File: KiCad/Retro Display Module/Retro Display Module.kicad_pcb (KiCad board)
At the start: 2 copper layers, 70 x 100 mm, 155 parts, among them J1 Conn_02x04_Odd_Even, J10 Conn_01x02_Pin, J11 Conn_01x02_Pin, J12 VCC, J13 TX, J14 RX, J15 CFG, J16 SEL, J17 GND, J18 Conn_01x12_Pin, J19 Conn_02x03_Odd_Even, J2 VCC, J20 Conn_01x02_Pin, J21 Conn_01x04_Pin, J22 Conn_01x02_Pin, J23 Conn_01x02_Pin, J24 Conn_01x02_Pin, J25 Conn_01x02_Pin, J26 Conn_01x02_Pin, J27 Conn_02x03_Odd_Even, J28 Conn_01x02_Pin, J29 Conn_01x04_Pin, J3 TX, J30 Conn_01x02_Pin, J31 Conn_02x03_Odd_Even, J32 Conn_01x02_Pin, J33 Conn_02x04_Odd_Even, J34 Conn_02x11_Odd_Even, J4 RX, J5 CFG, J6 SEL, J7 GND, J8 Conn_01x02_Pin, J9 Conn_01x02_Pin, U1 AO3401A, U10 AO3401A, U11 AO3401A, U12 LM358DR2G, U13 AO3401A, U14 AO3401A, U15 AO3401A, U16 AO3401A, U17 MJD44H11J, U18 AO3401A, U19 AO3401A, U2 AO3401A, U20 AO3401A, U21 AO3401A, U3 TS-1187A-B-A-B, U4 AO3401A, U5 STM32G030C8T6, U6 AO3401A, U7 TPS5430DDAR, U8 XC6206P332MR, U9 2N7002, Y1 Crystal

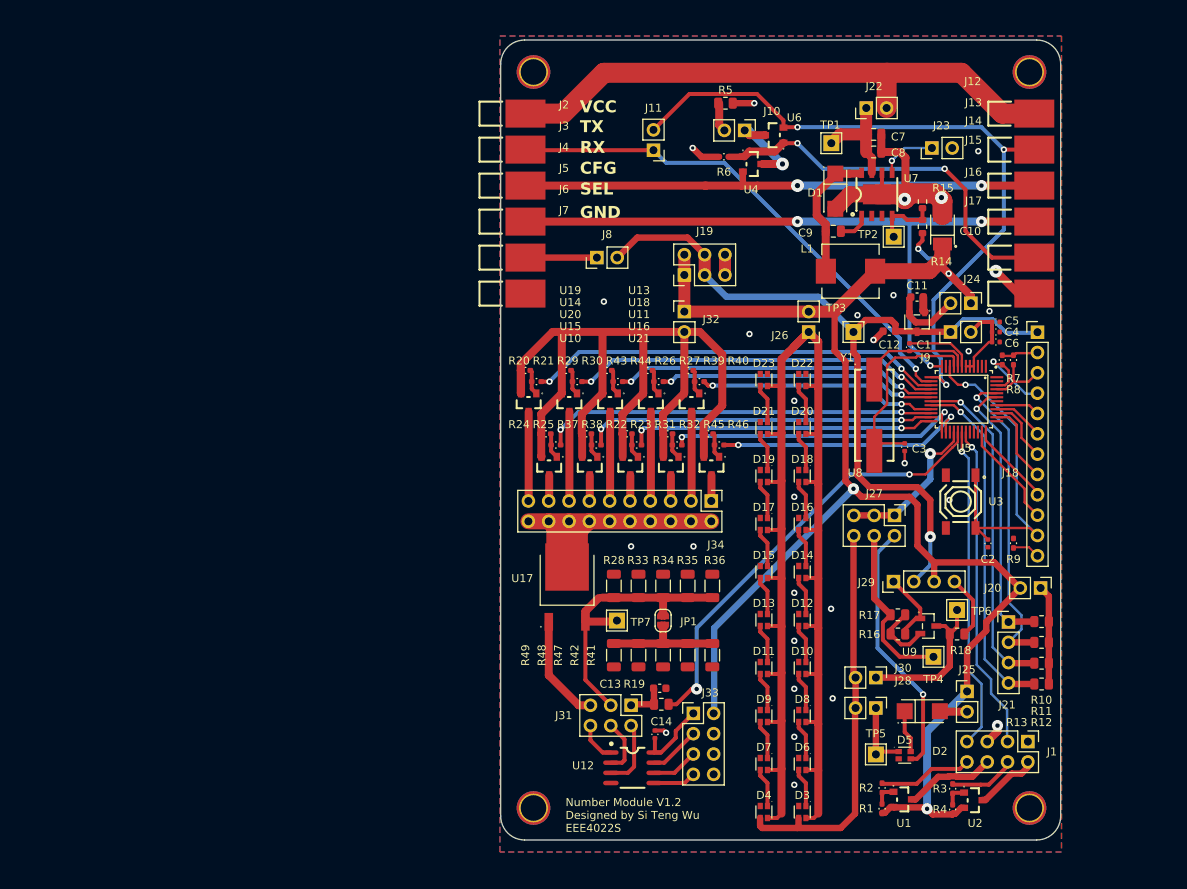
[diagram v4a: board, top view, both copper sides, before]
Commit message: Updated Schematics and Added Reverse polarity protection
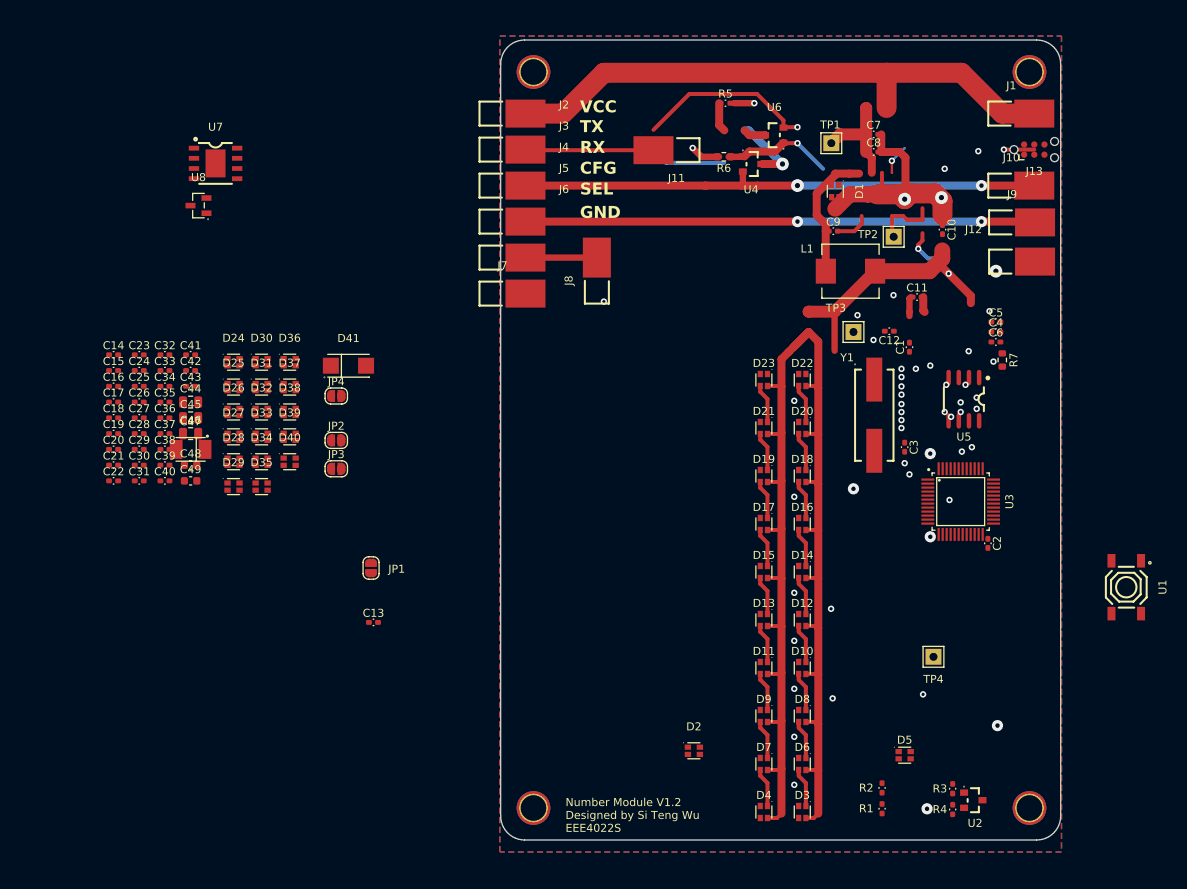
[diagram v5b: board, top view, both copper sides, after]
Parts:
- removed J14: RX, Library:CONN-SMD_YZF0002-38080-02
- removed J15: CFG, Library:CONN-SMD_YZF0002-38080-02
- removed J16: SEL, Library:CONN-SMD_YZF0002-38080-02
- removed J17: GND, Library:CONN-SMD_YZF0002-38080-02
- removed J18: Conn_01x12_Pin, Connector_PinHeader_2.54mm:PinHeader_1x12_P2.54mm_Vertical
- removed J19, J27, J31: Conn_02x03_Odd_Even, Connector_PinHeader_2.54mm:PinHeader_2x03_P2.54mm_Vertical
- removed J20, J22, J23, J24, J25, J26, J28, J30, J32: Conn_01x02_Pin, Connector_PinHeader_2.54mm:PinHeader_1x02_P2.54mm_Vertical
- removed J21, J29: Conn_01x04_Pin, Connector_PinHeader_2.54mm:PinHeader_1x04_P2.54mm_Vertical
- removed J33: Conn_02x04_Odd_Even, Connector_PinHeader_2.54mm:PinHeader_2x04_P2.54mm_Vertical
- removed J34: Conn_02x11_Odd_Even, Connector_PinHeader_2.54mm:PinHeader_2x10_P2.54mm_Vertical
- removed R10, R11, R12, R13: 4.7k, Resistor_SMD:R_0805_2012Metric
- removed R14: 12k, Resistor_SMD:R_0603_1608Metric
- removed R15: 3.9k, Resistor_SMD:R_0603_1608Metric
- removed R16, R17, R18: 1k, Resistor_SMD:R_0805_2012Metric
- removed R19: 10k, Resistor_SMD:R_0805_2012Metric
- removed R20, R22, R24, R26, R29, R31, R37, R39, R43, R45: 100k, Library:R_0402_1005Metric_Pad0.72x0.64mm_HandSolder
- removed R21, R23, R25, R27, R30, R32, R38, R40, R44, R46: 1k, Library:R_0402_1005Metric_Pad0.72x0.64mm_HandSolder
- removed R28, R33, R34, R35, R36, R41, R42, R47, R48, R49: 100, Resistor_SMD:R_1206_3216Metric
- removed R8, R9: 10k, Library:R_0402_1005Metric_Pad0.72x0.64mm_HandSolder
- removed TP5, TP6, TP7: TestPoint, Library:TestPoint_THTPad_2.0x2.0mm_Drill1.0mm
- removed U10, U11, U13, U14, U15, U16, U18, U19, U20, U21: AO3401A, Library:SOT-23_L2.9-W1.3-P1.90-LS2.4-BR
- removed U12: LM358DR2G, Library:Dual LM358
- removed U17: MJD44H11J, Library:MJD44 NPN
- removed U9: 2N7002, Library:SOT-23-3_L2.9-W1.3-P1.90-LS2.4-BR
- added C15: 0.1uF, Library:C_0402_1005Metric_Pad0.74x0.62mm_HandSolder, F.Cu at (67.5, 84.8)
- added C16: 0.1uF, Library:C_0402_1005Metric_Pad0.74x0.62mm_HandSolder, F.Cu at (67.5, 86.8)
- added C17: 0.1uF, Library:C_0402_1005Metric_Pad0.74x0.62mm_HandSolder, F.Cu at (67.5, 88.8)
- added C18: 0.1uF, Library:C_0402_1005Metric_Pad0.74x0.62mm_HandSolder, F.Cu at (67.5, 90.7)
- added C19: 0.1uF, Library:C_0402_1005Metric_Pad0.74x0.62mm_HandSolder, F.Cu at (67.5, 92.7)
- added C20: 0.1uF, Library:C_0402_1005Metric_Pad0.74x0.62mm_HandSolder, F.Cu at (67.5, 94.7)
- added C21: 0.1uF, Library:C_0402_1005Metric_Pad0.74x0.62mm_HandSolder, F.Cu at (67.5, 96.6)
- added C22: 0.1uF, Library:C_0402_1005Metric_Pad0.74x0.62mm_HandSolder, F.Cu at (67.5, 98.6)
- added C23: 0.1uF, Library:C_0402_1005Metric_Pad0.74x0.62mm_HandSolder, F.Cu at (70.7, 82.8)
- added C24: 0.1uF, Library:C_0402_1005Metric_Pad0.74x0.62mm_HandSolder, F.Cu at (70.7, 84.8)
- added C25: 0.1uF, Library:C_0402_1005Metric_Pad0.74x0.62mm_HandSolder, F.Cu at (70.7, 86.8)
- added C26: 0.1uF, Library:C_0402_1005Metric_Pad0.74x0.62mm_HandSolder, F.Cu at (70.7, 88.8)
- added C27: 0.1uF, Library:C_0402_1005Metric_Pad0.74x0.62mm_HandSolder, F.Cu at (70.7, 90.7)
- added C28: 0.1uF, Library:C_0402_1005Metric_Pad0.74x0.62mm_HandSolder, F.Cu at (70.7, 92.7)
- added C29: 0.1uF, Library:C_0402_1005Metric_Pad0.74x0.62mm_HandSolder, F.Cu at (70.7, 94.7)
- added C30: 0.1uF, Library:C_0402_1005Metric_Pad0.74x0.62mm_HandSolder, F.Cu at (70.7, 96.6)
- added C31: 0.1uF, Library:C_0402_1005Metric_Pad0.74x0.62mm_HandSolder, F.Cu at (70.7, 98.6)
- added C32: 0.1uF, Library:C_0402_1005Metric_Pad0.74x0.62mm_HandSolder, F.Cu at (73.9, 82.8)
- added C33: 0.1uF, Library:C_0402_1005Metric_Pad0.74x0.62mm_HandSolder, F.Cu at (73.9, 84.8)
- added C34: 0.1uF, Library:C_0402_1005Metric_Pad0.74x0.62mm_HandSolder, F.Cu at (73.9, 86.8)
- added C35: 0.1uF, Library:C_0402_1005Metric_Pad0.74x0.62mm_HandSolder, F.Cu at (73.9, 88.8)
- added C36: 0.1uF, Library:C_0402_1005Metric_Pad0.74x0.62mm_HandSolder, F.Cu at (73.9, 90.7)
- added C37: 0.1uF, Library:C_0402_1005Metric_Pad0.74x0.62mm_HandSolder, F.Cu at (73.9, 92.7)
- added C38: 0.1uF, Library:C_0402_1005Metric_Pad0.74x0.62mm_HandSolder, F.Cu at (73.9, 94.7)
- added C39: 0.1uF, Library:C_0402_1005Metric_Pad0.74x0.62mm_HandSolder, F.Cu at (73.9, 96.6)
- added C40: 0.1uF, Library:C_0402_1005Metric_Pad0.74x0.62mm_HandSolder, F.Cu at (73.9, 98.6)
- added C41: 0.1uF, Library:C_0402_1005Metric_Pad0.74x0.62mm_HandSolder, F.Cu at (77.1, 82.8)
- added C42: 0.1uF, Library:C_0402_1005Metric_Pad0.74x0.62mm_HandSolder, F.Cu at (77.1, 84.8)
- added C43: 0.1uF, Library:C_0402_1005Metric_Pad0.74x0.62mm_HandSolder, F.Cu at (77.1, 86.8)
- added C44: 4.7uF, Capacitor_SMD:C_0805_2012Metric, F.Cu at (77.1, 88.8)
- added C45: 4.7uF, Capacitor_SMD:C_0805_2012Metric, F.Cu at (77.1, 90.7)
- added C46: 10nF, Capacitor_SMD:C_0805_2012Metric, F.Cu at (77.1, 92.7)
- added C47: 220uF, Library:CAP-SMD_L3.5-W2.8, F.Cu at (77.1, 94.7)
- added C48: 1uF, Capacitor_SMD:C_0603_1608Metric, F.Cu at (77.1, 96.6)
- added C49: 1uF, Capacitor_SMD:C_0603_1608Metric, F.Cu at (77.1, 98.6)
- added D24: XL-1615RGBC-WS2812B, Library:LED-SMD_4P-L1.6-W1.5_XL-1615RGBC-WS2812B, F.Cu at (82.5, 83.8)
- added D25: XL-1615RGBC-WS2812B, Library:LED-SMD_4P-L1.6-W1.5_XL-1615RGBC-WS2812B, F.Cu at (82.5, 86.9)
- added D26: XL-1615RGBC-WS2812B, Library:LED-SMD_4P-L1.6-W1.5_XL-1615RGBC-WS2812B, F.Cu at (82.5, 90.0)
- added D27: XL-1615RGBC-WS2812B, Library:LED-SMD_4P-L1.6-W1.5_XL-1615RGBC-WS2812B, F.Cu at (82.5, 93.1)
- added D28: XL-1615RGBC-WS2812B, Library:LED-SMD_4P-L1.6-W1.5_XL-1615RGBC-WS2812B, F.Cu at (82.5, 96.2)
- added D29: XL-1615RGBC-WS2812B, Library:LED-SMD_4P-L1.6-W1.5_XL-1615RGBC-WS2812B, F.Cu at (82.5, 99.3)
- added D30: XL-1615RGBC-WS2812B, Library:LED-SMD_4P-L1.6-W1.5_XL-1615RGBC-WS2812B, F.Cu at (86.0, 83.8)
- added D31: XL-1615RGBC-WS2812B, Library:LED-SMD_4P-L1.6-W1.5_XL-1615RGBC-WS2812B, F.Cu at (86.0, 86.9)
- added D32: XL-1615RGBC-WS2812B, Library:LED-SMD_4P-L1.6-W1.5_XL-1615RGBC-WS2812B, F.Cu at (86.0, 90.0)
- added D33: XL-1615RGBC-WS2812B, Library:LED-SMD_4P-L1.6-W1.5_XL-1615RGBC-WS2812B, F.Cu at (86.0, 93.1)
- added D34: XL-1615RGBC-WS2812B, Library:LED-SMD_4P-L1.6-W1.5_XL-1615RGBC-WS2812B, F.Cu at (86.0, 96.2)
- added D35: XL-1615RGBC-WS2812B, Library:LED-SMD_4P-L1.6-W1.5_XL-1615RGBC-WS2812B, F.Cu at (86.0, 99.3)
- added D36: XL-1615RGBC-WS2812B, Library:LED-SMD_4P-L1.6-W1.5_XL-1615RGBC-WS2812B, F.Cu at (89.5, 83.8)
- added D37: XL-1615RGBC-WS2812B, Library:LED-SMD_4P-L1.6-W1.5_XL-1615RGBC-WS2812B, F.Cu at (89.5, 86.9)
- added D38: XL-1615RGBC-WS2812B, Library:LED-SMD_4P-L1.6-W1.5_XL-1615RGBC-WS2812B, F.Cu at (89.5, 90.0)
- added D39: XL-1615RGBC-WS2812B, Library:LED-SMD_4P-L1.6-W1.5_XL-1615RGBC-WS2812B, F.Cu at (89.5, 93.1)
- added D40: XL-1615RGBC-WS2812B, Library:LED-SMD_4P-L1.6-W1.5_XL-1615RGBC-WS2812B, F.Cu at (89.5, 96.2)
- added D41: SS34, Library:SMA_L4.3-W2.6-LS5.2-RD, F.Cu at (96.9, 84.2)
- added JP2: Jumper_2_Open, Jumper:SolderJumper-2_P1.3mm_Open_RoundedPad1.0x1.5mm, F.Cu at (95.3, 93.5)
- added JP3: Jumper_2_Open, Jumper:SolderJumper-2_P1.3mm_Open_RoundedPad1.0x1.5mm, F.Cu at (95.3, 97.1)
- added JP4: Jumper_2_Open, Jumper:SolderJumper-2_P1.3mm_Open_RoundedPad1.0x1.5mm, F.Cu at (95.3, 88.0)
- C1, C14, C2, C3, C4: footprint Library:C_0402_1005Metric -> Library:C_0402_1005Metric_Pad0.74x0.62mm_HandSolder
- C10: value 220uF -> 0.1uF; footprint Library:CAP-SMD_L3.5-W2.8 -> Library:C_0402_1005Metric_Pad0.74x0.62mm_HandSolder
- C11, C12, C13: value 1uF -> 0.1uF; footprint Capacitor_SMD:C_0603_1608Metric -> Library:C_0402_1005Metric_Pad0.74x0.62mm_HandSolder
- C5: value 4.7uF -> 0.1uF; footprint Library:C_0402_1005Metric -> Library:C_0402_1005Metric_Pad0.74x0.62mm_HandSolder
- C6: value 0.1uF -> 4.7uF; footprint Library:C_0402_1005Metric -> Library:C_0402_1005Metric_Pad0.74x0.62mm_HandSolder
- C7, C8: value 4.7uF -> 0.1uF; footprint Capacitor_SMD:C_0805_2012Metric -> Library:C_0402_1005Metric_Pad0.74x0.62mm_HandSolder
- C9: value 10nF -> 0.1uF; footprint Capacitor_SMD:C_0805_2012Metric -> Library:C_0402_1005Metric_Pad0.74x0.62mm_HandSolder
- D1: value SS34 -> XL-1615RGBC-WS2812B; footprint Library:SMA_L4.3-W2.6-LS5.2-RD -> Library:LED-SMD_4P-L1.6-W1.5_XL-1615RGBC-WS2812B
- D2: value M7 -> XL-1615RGBC-WS2812B; footprint Library:SMA_L4.3-W2.6-LS5.2-RD -> Library:LED-SMD_4P-L1.6-W1.5_XL-1615RGBC-WS2812B
- J1: value Conn_02x04_Odd_Even -> VCC; footprint Connector_PinHeader_2.54mm:PinHeader_2x04_P2.54mm_Vertical -> Library:CONN-SMD_YZF0002-38080-02
- J10: value Conn_01x02_Pin -> CFG; footprint Connector_PinHeader_2.54mm:PinHeader_1x02_P2.54mm_Vertical -> Library:CONN-SMD_YZF0002-38080-02
- J11: value Conn_01x02_Pin -> SEL; footprint Connector_PinHeader_2.54mm:PinHeader_1x02_P2.54mm_Vertical -> Library:CONN-SMD_YZF0002-38080-02
- J12: value VCC -> GND
- J13: value TX -> Conn_02x03_Odd_Even; footprint Library:CONN-SMD_YZF0002-38080-02 -> Connector:Tag-Connect_TC2030-IDC-NL_2x03_P1.27mm_Vertical
- J2: value VCC -> TX
- J3: value TX -> RX
- J4: value RX -> CFG
- J5: value CFG -> SEL
- J6: value SEL -> GND
- J7: value GND -> VCC
- J8: value Conn_01x02_Pin -> TX; footprint Connector_PinHeader_2.54mm:PinHeader_1x02_P2.54mm_Vertical -> Library:CONN-SMD_YZF0002-38080-02
- J9: value Conn_01x02_Pin -> RX; footprint Connector_PinHeader_2.54mm:PinHeader_1x02_P2.54mm_Vertical -> Library:CONN-SMD_YZF0002-38080-02
- R4: value 100k -> 10k
- R5: footprint Resistor_SMD:R_0805_2012Metric -> Library:R_0402_1005Metric_Pad0.72x0.64mm_HandSolder
- R6: value 100k -> 12k; footprint Library:R_0402_1005Metric_Pad0.72x0.64mm_HandSolder -> Resistor_SMD:R_0603_1608Metric
- R7: value 10k -> 3.9k; footprint Library:R_0402_1005Metric_Pad0.72x0.64mm_HandSolder -> Resistor_SMD:R_0603_1608Metric
- U1: value AO3401A -> TS-1187A-B-A-B; footprint Library:SOT-23_L2.9-W1.3-P1.90-LS2.4-BR -> Library:SW-SMD_4P-L5.1-W5.1-P3.70-LS6.5-TL-2
- U3: value TS-1187A-B-A-B -> STM32G030C8T6; footprint Library:SW-SMD_4P-L5.1-W5.1-P3.70-LS6.5-TL-2 -> Library:LQFP-48_L7.0-W7.0-P0.50-LS9.0-BL_1
- U5: value STM32G030C8T6 -> LM358; footprint Library:LQFP-48_L7.0-W7.0-P0.50-LS9.0-BL_1 -> Library:Dual LM358
- U8: footprint Library:XC6206 -> Library:SOT-23-3_L2.9-W1.3-P1.90-LS2.4-BR
- moved U8 91.0 mm to (78.1, 64.2), turned to 0 degrees
- moved U7 82.8 mm to (80.3, 58.9), turned to 0 degrees
- moved C14 82.6 mm to (67.5, 82.8), turned to 0 degrees
- moved J1 78.5 mm to (182.6, 52.7), turned to 0 degrees
- moved U1 38.5 mm to (194.1, 111.9), turned to -90 degrees
- moved JP1 37.1 mm to (99.7, 109.5)
- moved J10 36.9 mm to (182.6, 61.7), turned to 0 degrees
- moved C13 36.7 mm to (100.0, 116.3)
- moved D2 29.0 mm to (140.0, 132.3)
- moved J12 18.5 mm to (182.7, 71.2)
- moved J9 17.3 mm to (182.7, 66.3), turned to 0 degrees
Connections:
- C1 pad 1: Net-(U5-PF0-OSC_IN) -> Net-(U3-PF0-OSC_IN)
- C11 pad 1: Net-(J24-Pin_2) -> /5V
- C12 pad 1: /3V3 -> /5V
- C13 pad 1: Net-(J31-Pin_1) -> /5V
- C14 pad 1: Net-(J33-Pin_1) -> /5V
- C3 pad 1: Net-(U5-PF1-OSC_OUT) -> Net-(U3-PF1-OSC_OUT)
- C4 pad 1: /VR/B -> /3V3
- C5 pad 1: /VR/B -> Net-(J11-Pin_1)
- C6 pad 1: /VR/B -> /3V3
- C7 pad 1: Net-(J22-Pin_1) -> /3V3
- C8 pad 1: Net-(J22-Pin_1) -> /5V
- C9 pad 1: Net-(D1-K) -> /5V
- C9 pad 2: Net-(U7-BOOT) -> GND
- D1 pad 1: Net-(D1-K) -> Net-(D1-DO)
- D1 pad 2: GND -> /5V
- D10 pad 2: Net-(D10-VDD) -> /5V
- D11 pad 2: Net-(D10-VDD) -> /5V
- D12 pad 2: Net-(D10-VDD) -> /5V
- D12 pad 4: Net-(D10-DO) -> Net-(D12-DI)
- D13 pad 2: Net-(D10-VDD) -> /5V
- D13 pad 4: Net-(D11-DO) -> Net-(D13-DI)
- D14 pad 2: Net-(D10-VDD) -> /5V
- D14 pad 4: Net-(D12-DO) -> Net-(D10-DO)
- D15 pad 2: Net-(D10-VDD) -> /5V
- D15 pad 4: Net-(D13-DO) -> Net-(D11-DO)
- D16 pad 2: Net-(D10-VDD) -> /5V
- D16 pad 4: Net-(D14-DO) -> Net-(D12-DO)
- D17 pad 2: Net-(D10-VDD) -> /5V
- D17 pad 4: Net-(D15-DO) -> Net-(D13-DO)
- D18 pad 2: Net-(D10-VDD) -> /5V
- D18 pad 4: Net-(D16-DO) -> Net-(D14-DO)
- D19 pad 2: Net-(D10-VDD) -> /5V
- D19 pad 4: Net-(D17-DO) -> Net-(D15-DO)
- D2 pad 1: Net-(D2-K) -> Net-(D2-DO)
- D2 pad 2: Net-(D2-A) -> /5V
- D20 pad 2: Net-(D10-VDD) -> /5V
- D20 pad 4: Net-(D18-DO) -> Net-(D16-DO)
- D21 pad 2: Net-(D10-VDD) -> /5V
- D21 pad 4: Net-(D19-DO) -> Net-(D17-DO)
- D22 pad 1: unconnected-(D22-DO-Pad1) -> Net-(D22-DO)
- D22 pad 2: Net-(D10-VDD) -> /5V
- D22 pad 4: Net-(D20-DO) -> Net-(D18-DO)
- D23 pad 1: unconnected-(D23-DO-Pad1) -> Net-(D23-DO)
- D23 pad 2: Net-(D10-VDD) -> /5V
- D23 pad 4: Net-(D21-DO) -> Net-(D19-DO)
- D3 pad 2: Net-(D10-VDD) -> /5V
- D3 pad 4: /RGB LEDs/DIN -> /TIM1_CH1
- D4 pad 2: Net-(D10-VDD) -> /5V
- D4 pad 4: /RGB LEDs/DIN -> /TIM1_CH1
- D5 pad 2: Net-(D2-K) -> /5V
- D5 pad 4: /RGB LEDs/Cheese -> Net-(D1-DO)
- D6 pad 1: Net-(D6-DO) -> Net-(D10-DI)
- D6 pad 2: Net-(D10-VDD) -> /5V
- D6 pad 4: Net-(D3-DO) -> Net-(D2-DO)
- D7 pad 1: Net-(D7-DO) -> Net-(D11-DI)
- D7 pad 2: Net-(D10-VDD) -> /5V
- D7 pad 4: Net-(D4-DO) -> Net-(D3-DO)
- D8 pad 1: Net-(D10-DI) -> Net-(D12-DI)
- D8 pad 2: Net-(D10-VDD) -> /5V
- D8 pad 4: Net-(D6-DO) -> Net-(D4-DO)
- D9 pad 1: Net-(D11-DI) -> Net-(D13-DI)
- D9 pad 2: Net-(D10-VDD) -> /5V
- D9 pad 4: Net-(D7-DO) -> Net-(D5-DO)
- J1 pad 1: GND -> /VCC
- J10 pad 1: Net-(J10-Pin_1) -> /PA1
- J11 pad 1: /USART2_Rx -> Net-(J11-Pin_1)
- J12 pad 1: /VCC -> GND
- J13 pad 1: /USART2_Tx -> /3V3
- J2 pad 1: /VCC -> /USART2_Rx
- J3 pad 1: /USART2_Rx -> Net-(J3-Pin_1)
- J4 pad 1: Net-(J14-Pin_1) -> /PA1
- J5 pad 1: /PA1 -> /3V3
- J6 pad 1: Net-(J6-Pin_1) -> GND
- J7 pad 1: GND -> /VCC
- J8 pad 1: Net-(J6-Pin_1) -> /USART2_Tx
- J9 pad 1: /3V3 -> Net-(J3-Pin_1)
- JP1 pad 1: /LED Driver/-ve -> /5V
- JP1 pad 2: Net-(JP1-B) -> /Power/5V
- L1 pad 1: Net-(D1-K) -> Net-(D41-K)
- L1 pad 2: /5V -> /Power/5V
- R1 pad 1: /5V -> Net-(J11-Pin_1)
- R1 pad 2: Net-(U1-G) -> GND
- R2 pad 1: Net-(U1-G) -> /USART2_Rx
- R2 pad 2: /PC6 -> Net-(U3-PA3)
- R3 pad 1: Net-(U2-G) -> /USART2_Tx
- R3 pad 2: /PC7 -> Net-(U3-PA2)
- R4 pad 1: /5V -> GND
- R4 pad 2: Net-(U2-G) -> /SWDCLK/BOOT
- R5 pad 1: Net-(J10-Pin_2) -> /PA1
- R5 pad 2: GND -> Net-(U3-PA1)
- R6 pad 1: Net-(J16-Pin_1) -> /Power/5V
- R6 pad 2: GND -> Net-(U7-VSENSE)
- R7 pad 1: /I2C_PUR -> Net-(U7-VSENSE)
- R7 pad 2: /I2C1_SDA -> GND
- TP1 pad 1: Net-(J22-Pin_1) -> Net-(U5A-+)
- TP3 pad 1: /3V3 -> /Power/5V
- TP4 pad 1: /RGB LEDs/Level -> /Power/3V3
- U1 pad 1: Net-(U1-G) -> /NRST
- U1 pad 2: /5V -> /NRST
- U1 pad 3: Net-(J1-Pin_6) -> GND
- U2 pad 1: Net-(U2-G) -> Net-(J11-Pin_1)
- U2 pad 2: /5V -> Net-(J3-Pin_1)
- U2 pad 3: Net-(J1-Pin_2) -> Net-(U2-D)
- U3 pad 1: /NRST -> unconnected-(U3-PC13-Pad1)
- U3 pad 2: /NRST -> unconnected-(U3-PC14-OSC32_IN-Pad2)
- U3 pad 3: GND -> unconnected-(U3-PC15-OSC32_OUT-Pad3)
- U3 pad 4: GND -> /3V3
- U4 pad 1: Net-(J16-Pin_1) -> Net-(J11-Pin_1)
- U4 pad 2: Net-(J14-Pin_1) -> /USART2_Tx
- U4 pad 3: Net-(J10-Pin_1) -> Net-(U2-D)
- U5 pad 1: unconnected-(U5-PC13-Pad1) -> Net-(U6-G)
- U5 pad 2: unconnected-(U5-PC14-OSC32_IN-Pad2) -> /Power/VCC
- U5 pad 3: unconnected-(U5-PC15-OSC32_OUT-Pad3) -> Net-(U5A-+)
- U5 pad 4: /VR/B -> GND
- U5 pad 5: /VR/B -> GND
- U5 pad 6: /VR/B -> GND
- U5 pad 7: GND -> unconnected-(U5-Pad7)
- U5 pad 8: Net-(U5-PF0-OSC_IN) -> Net-(U5A-+)
- U6 pad 1: Net-(J16-Pin_1) -> Net-(U6-G)
- U6 pad 2: /USART2_Tx -> Net-(U5A-+)
- U6 pad 3: Net-(J10-Pin_1) -> /Power/VCC
- U7 pad 7: Net-(J22-Pin_1) -> Net-(U5A-+)
- U7 pad 8: Net-(D1-K) -> Net-(D41-K)
- U8 pad 2: Net-(J24-Pin_2) -> /Power/3V3
- U8 pad 3: /3V3 -> /Power/5V
- Y1 pad 1: Net-(U5-PF0-OSC_IN) -> Net-(U3-PF0-OSC_IN)
- Y1 pad 2: Net-(U5-PF1-OSC_OUT) -> Net-(U3-PF1-OSC_OUT)
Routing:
- net Net-(D10-VDD): track 159.4 -> 0.00 mm
- net /PA1: track 141.0 -> 3.67 mm, vias 3 -> 0
- net (no net): track 0.00 -> 126.9 mm, vias 0 -> 11
- net /LED Driver/5V_PWR: track 115.0 -> 0.00 mm
- net /USART2_Tx: track 88.9 -> 3.80 mm
- net Net-(J14-Pin_1): track 65.6 -> 0.00 mm, vias 2 -> 0
- net /LED Driver/main_col: track 65.4 -> 0.00 mm
- net /TIM1_CH2: track 55.5 -> 0.00 mm, vias 2 -> 0
- net /PA4: track 52.0 -> 0.00 mm, vias 2 -> 0
- net /NRST: track 50.3 -> 0.00 mm, vias 1 -> 0
- net /RGB LEDs/DIN: track 49.9 -> 0.00 mm
- net /PB10: track 49.2 -> 0.00 mm, vias 2 -> 0
- net Net-(J16-Pin_1): track 47.7 -> 0.00 mm, vias 2 -> 0
- net /PA5: track 46.3 -> 0.00 mm, vias 2 -> 0
- net /PB11: track 43.9 -> 0.00 mm, vias 2 -> 0
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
